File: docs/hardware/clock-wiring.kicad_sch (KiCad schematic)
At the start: 6 parts, among them U1 ESP32 USB-C, U2 5 V logic buffer*, U3 MAX7219 / INPUT, U4 AHT20 + BMP280, U5 NS4168 amplifier

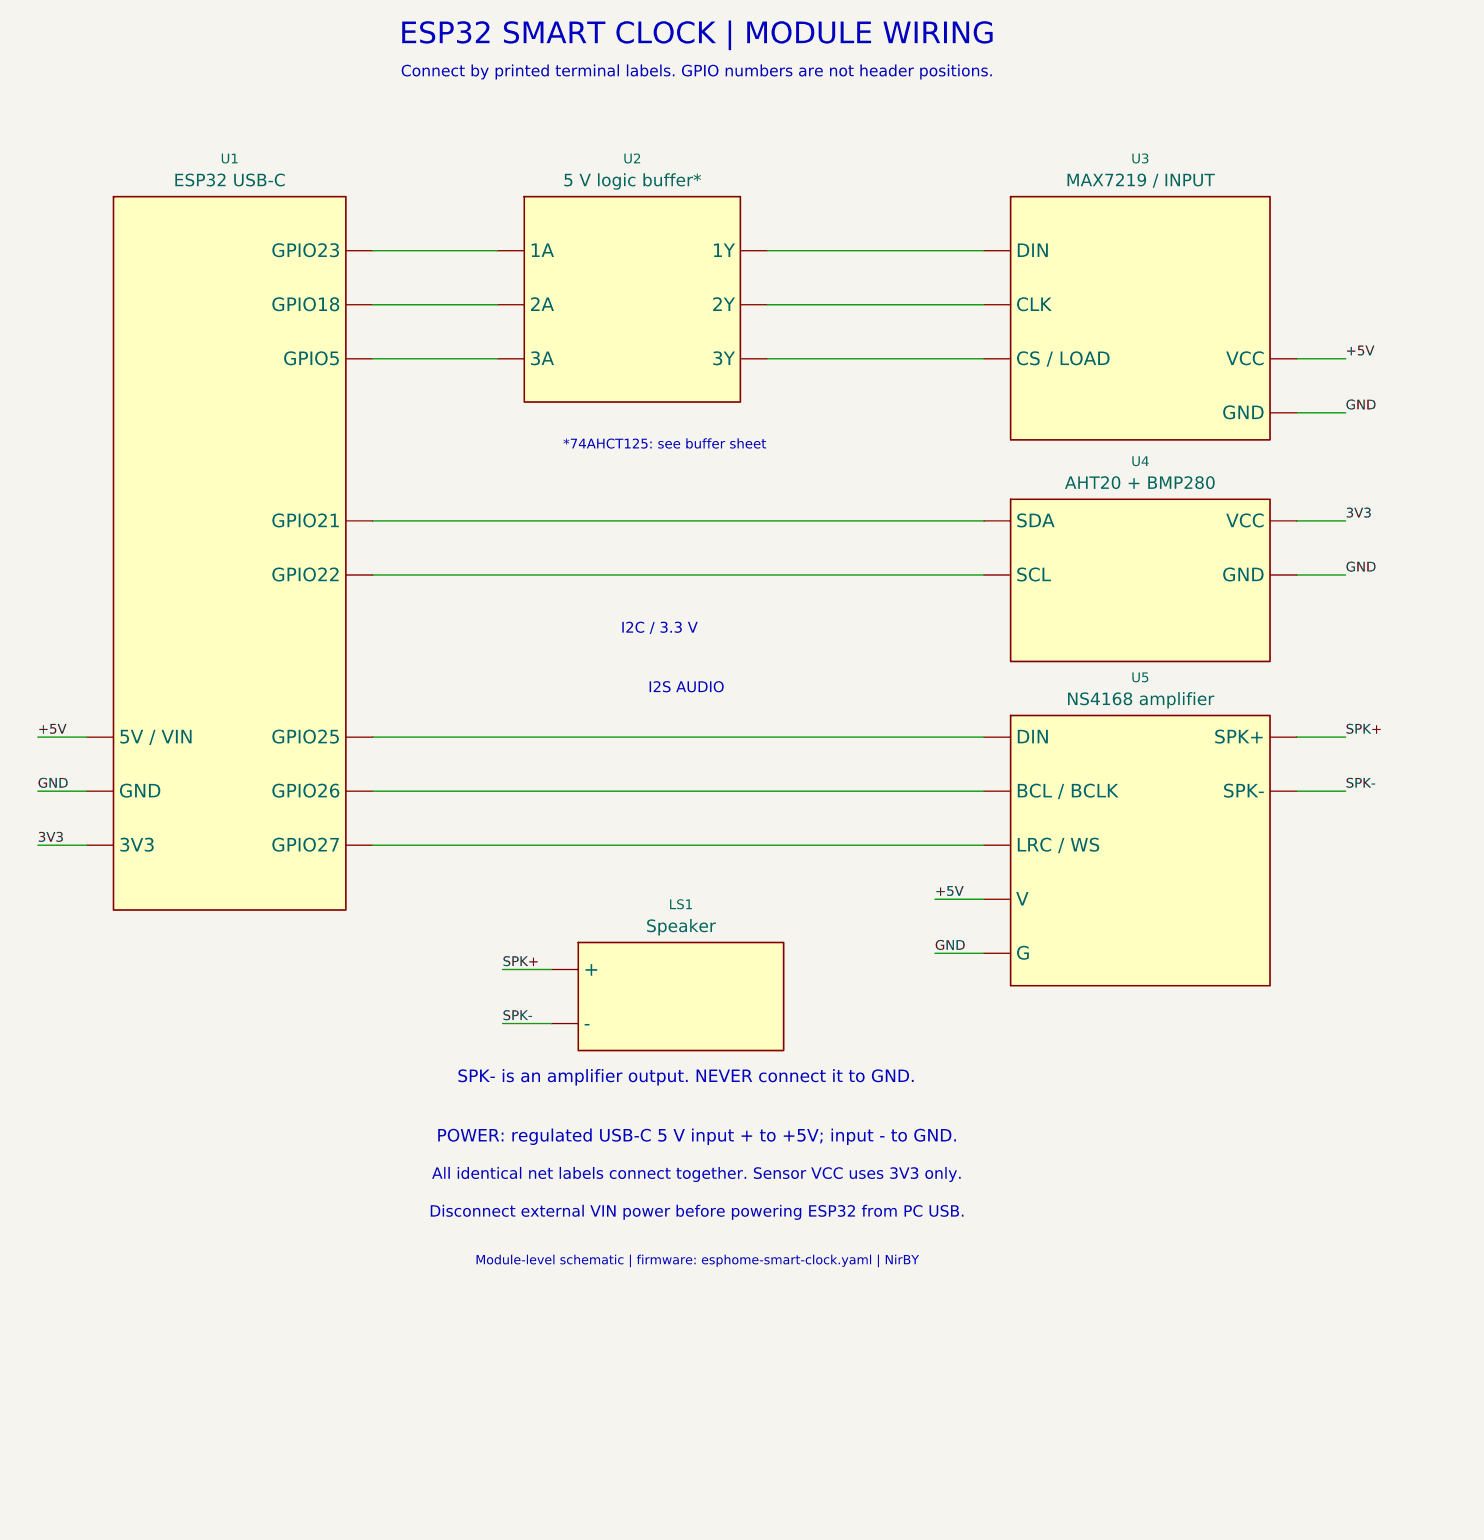
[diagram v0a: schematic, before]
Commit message: Show both USB-C connectors explicitly in wiring diagram
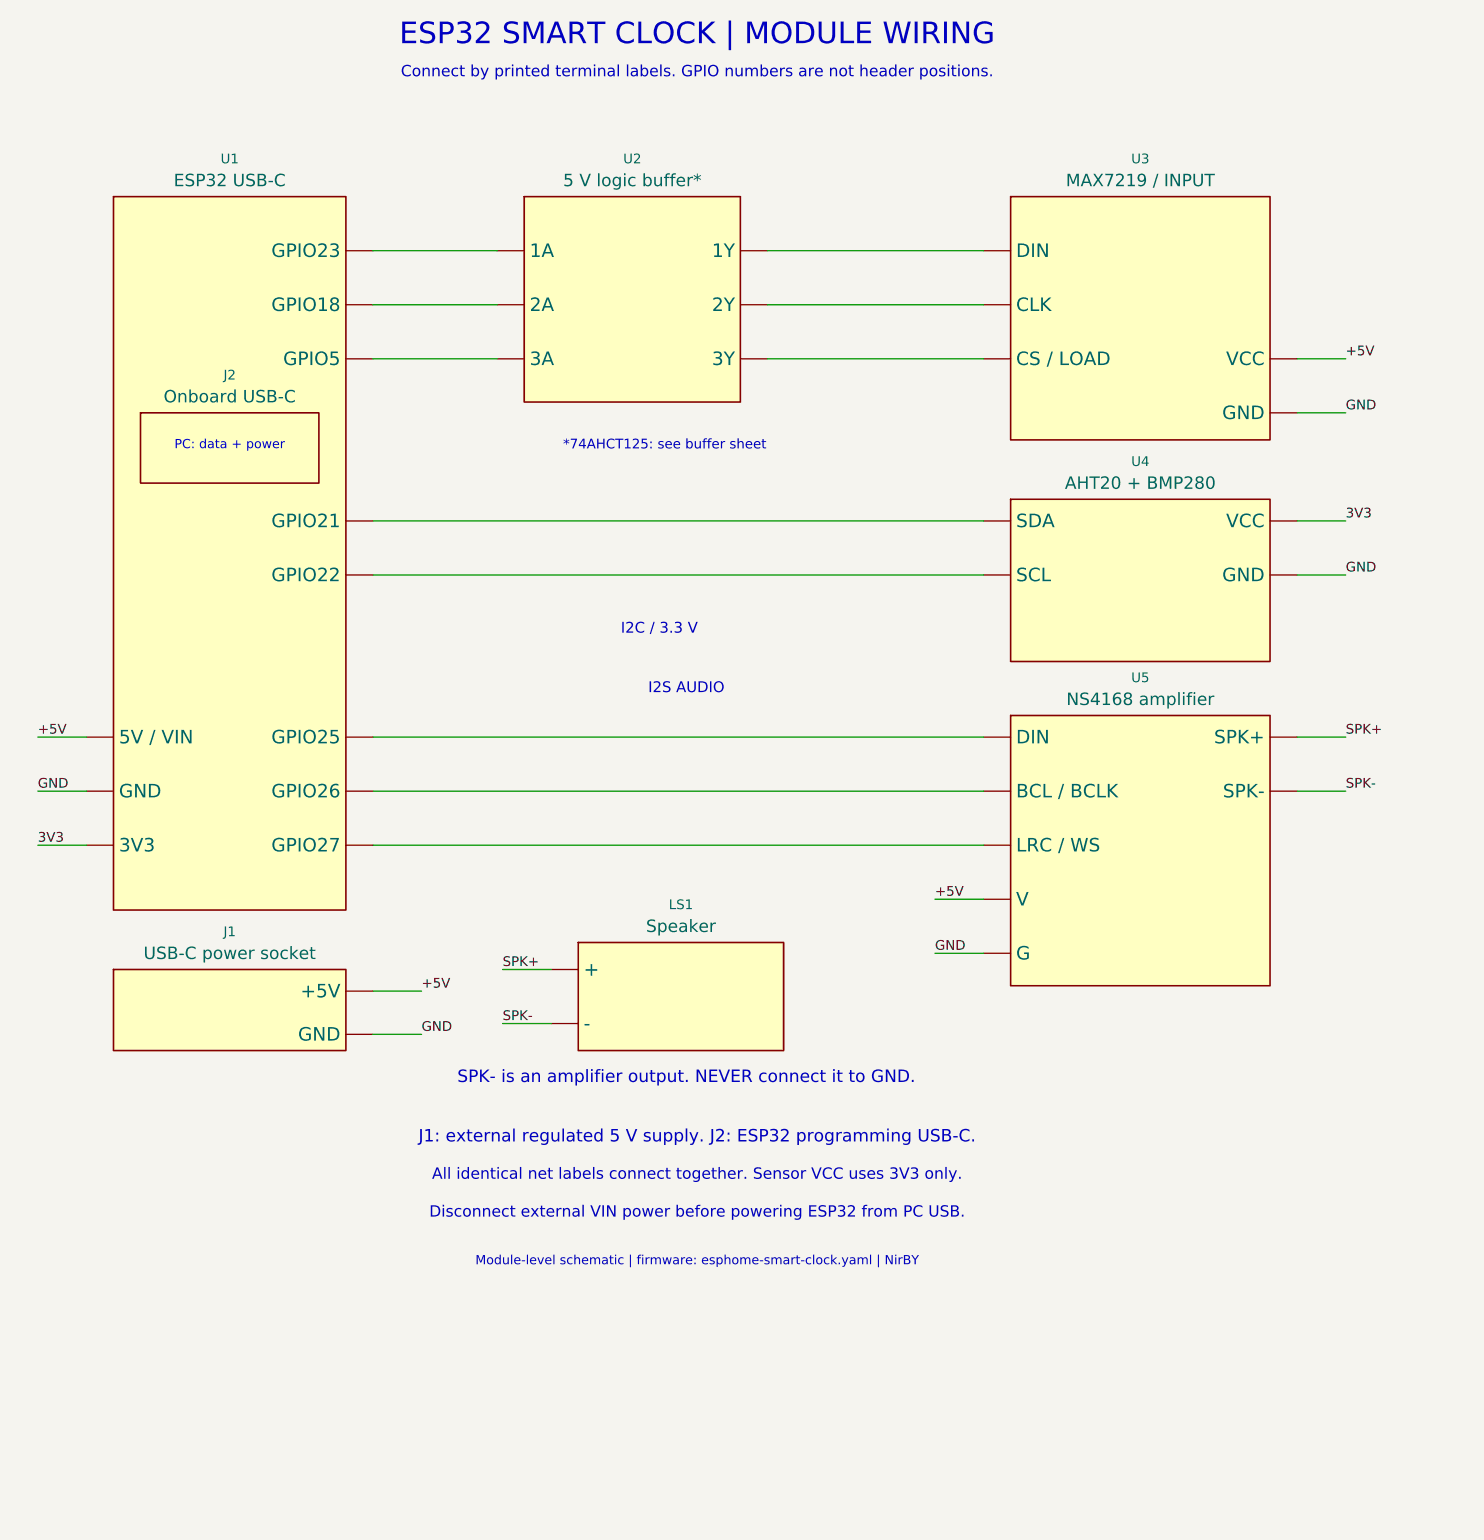
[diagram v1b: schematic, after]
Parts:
- added J1: USB-C power socket, symbol Clock:J1_module
- added J2: Onboard USB-C, symbol Clock:J2_module
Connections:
- net +5V: now also J1.1 (+5V)
- net GND: now also J1.2 (GND)
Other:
- note added: "J1: external regulated 5 V supply. J2: ESP32 programming USB-C."
- note added: "PC: data + power"
- note removed: "POWER: regulated USB-C 5 V input + to +5V; input - to GND."

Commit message: Remove nonexistent U2 and document direct MAX7219 wiring
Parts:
- removed U2: 5 V logic buffer*, symbol Clock:U2_module
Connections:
- net at U1.1 (GPIO23): now also U3.1 (DIN)
- net at U1.2 (GPIO18): now also U3.2 (CLK)
- net at U1.3 (GPIO5): now also U3.3 (CS / LOAD)
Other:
- note added: "DIRECT DISPLAY SIGNALS"
- note removed: "*74AHCT125: see buffer sheet"

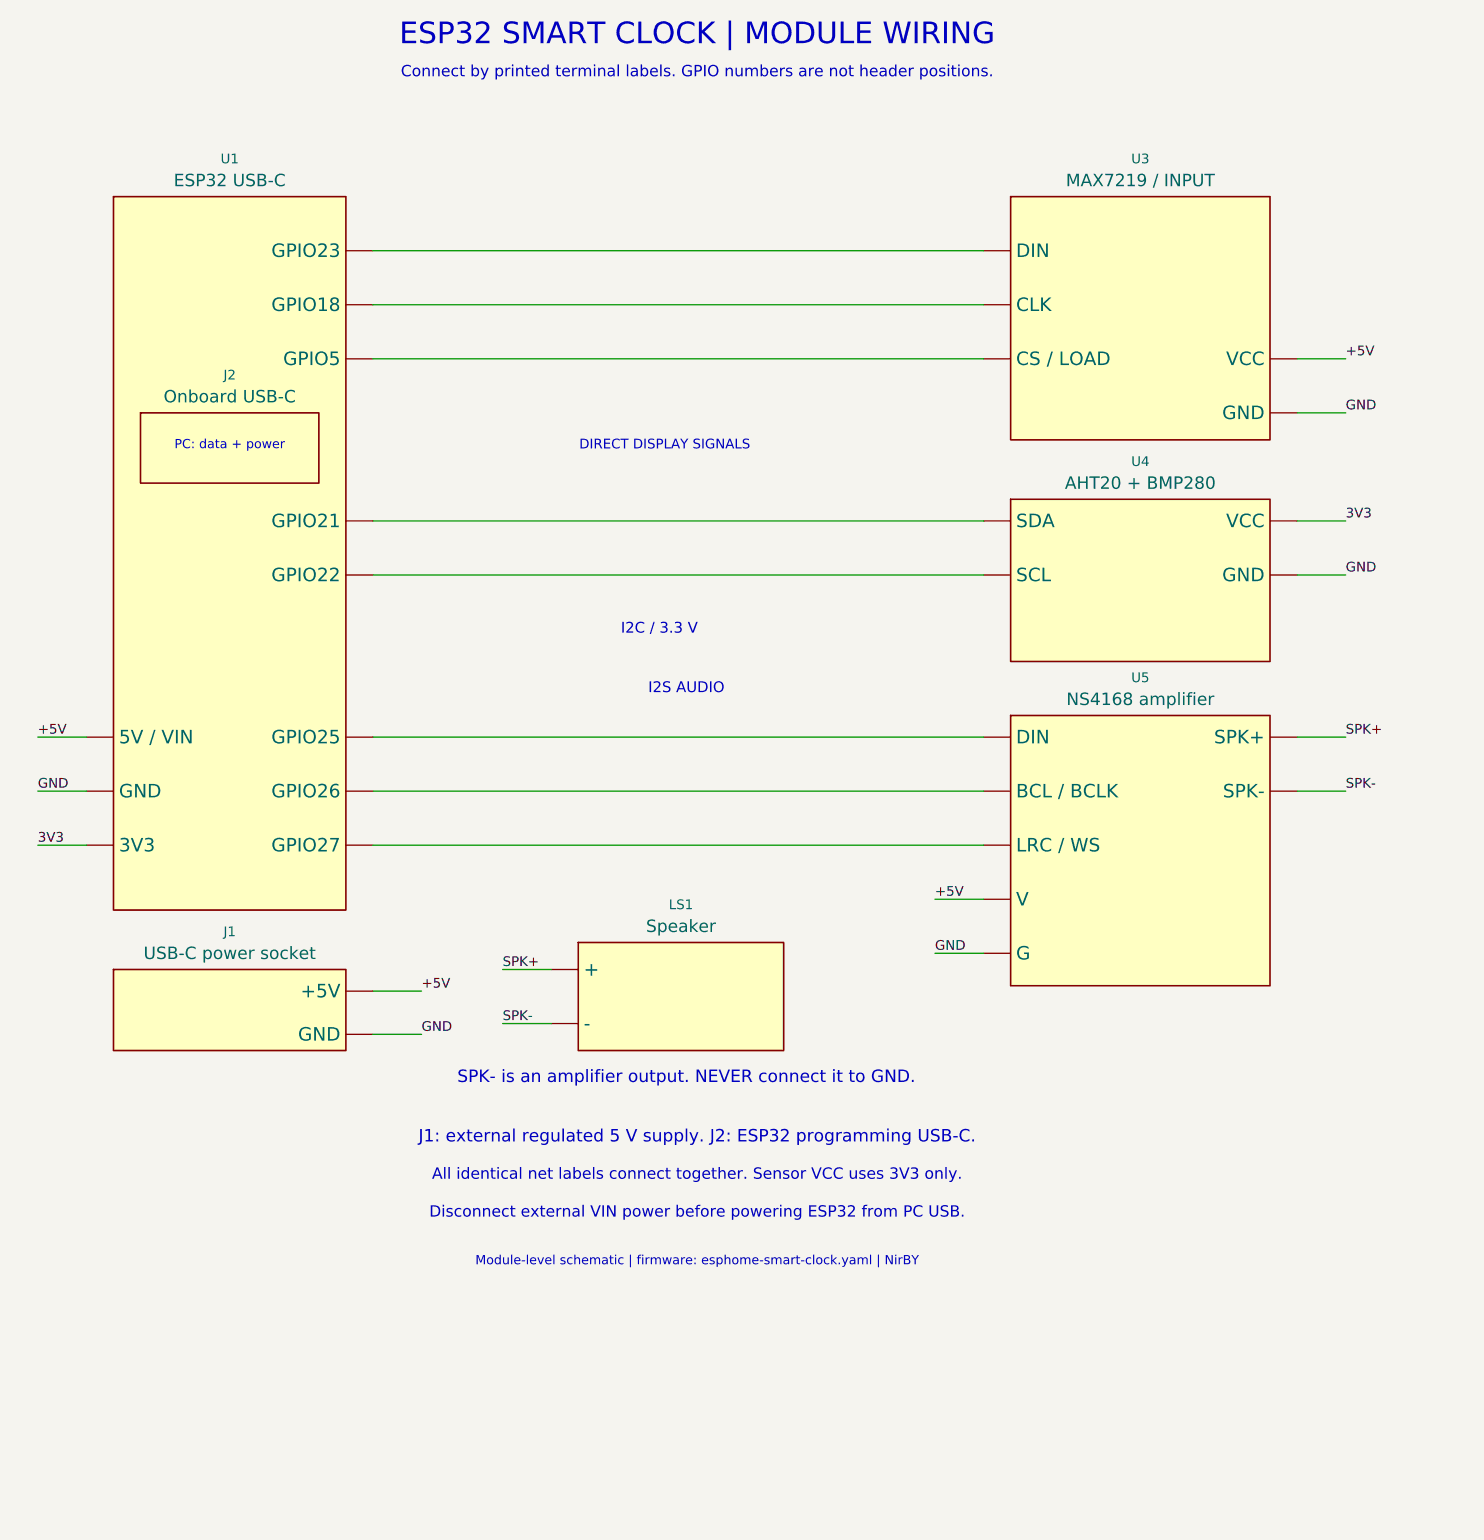
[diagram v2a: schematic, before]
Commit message: Connect USB-C power visibly to all loads in main wiring diagram
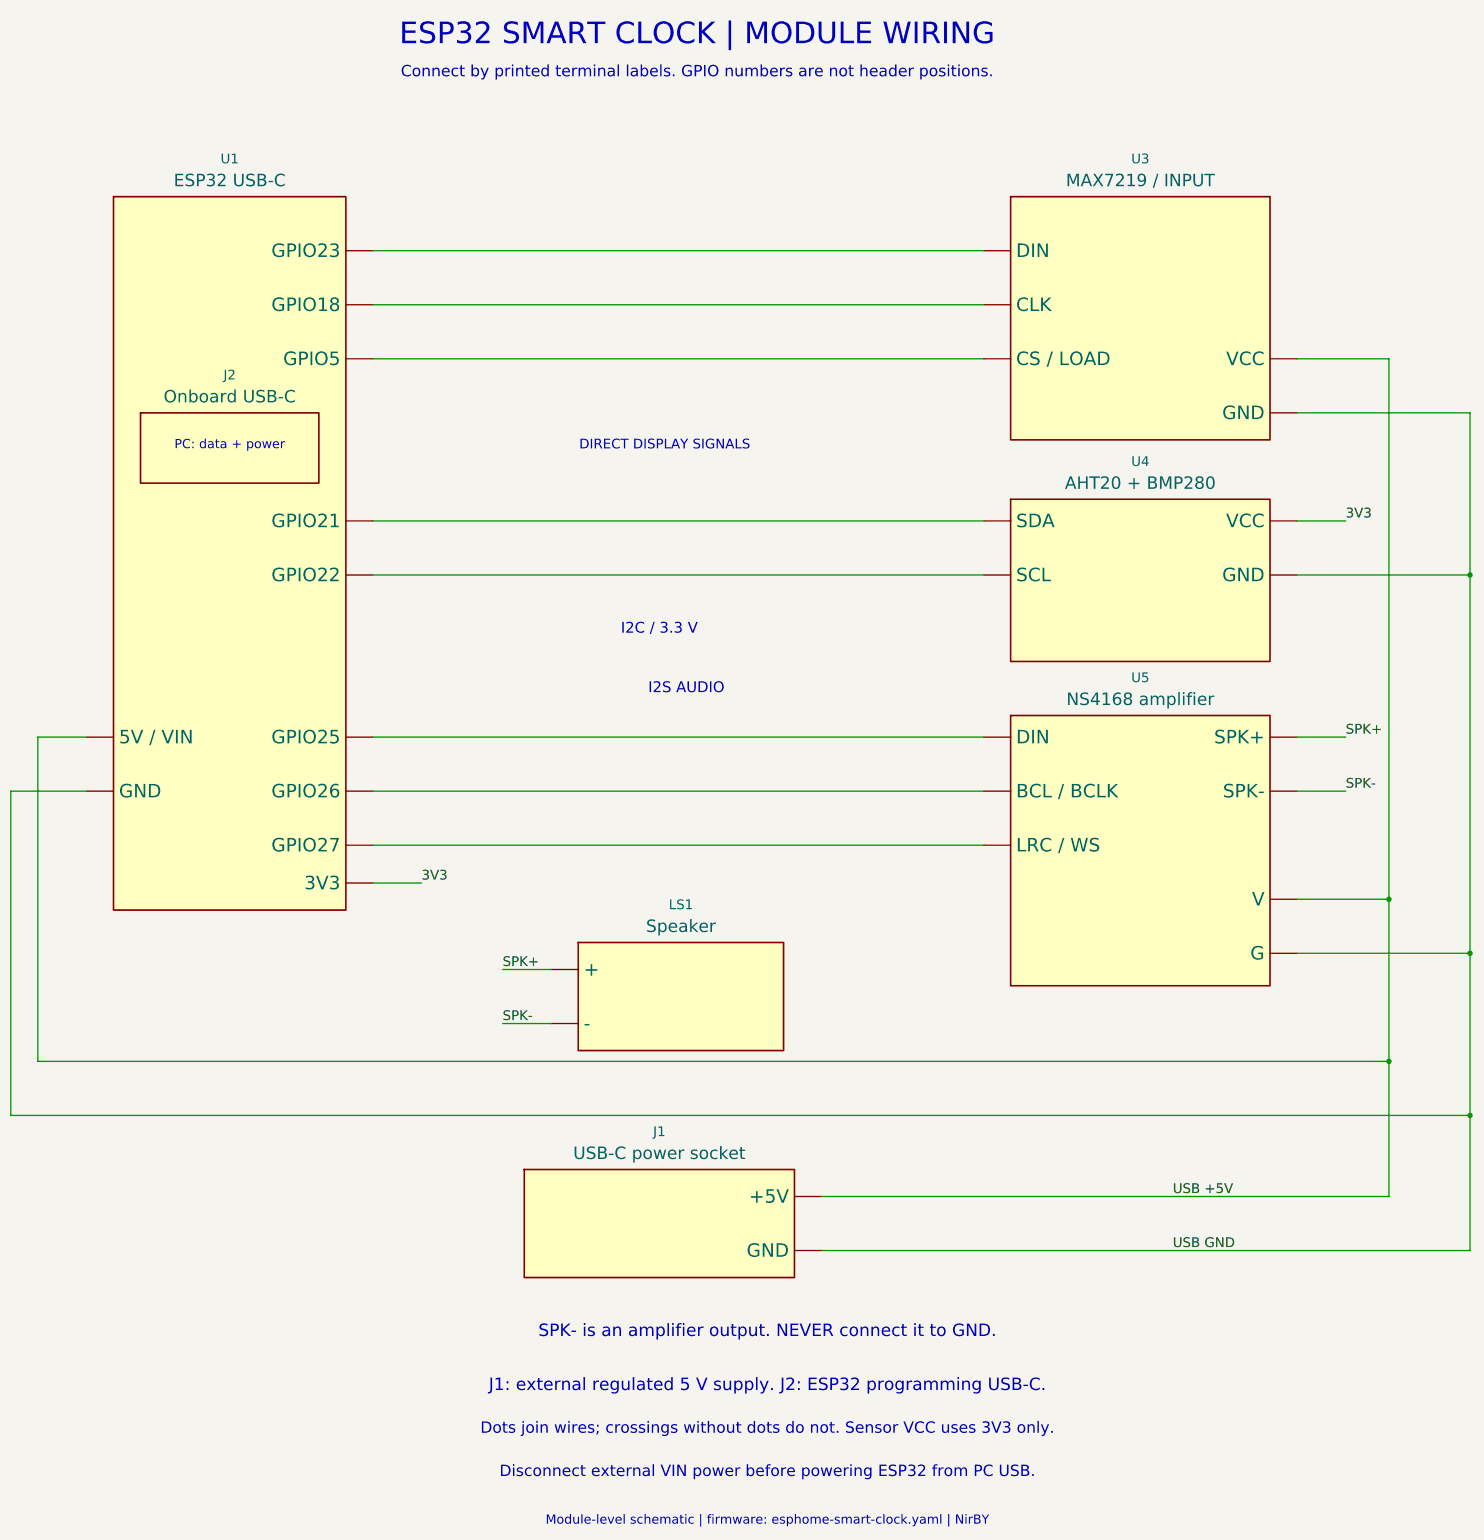
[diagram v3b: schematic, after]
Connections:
- net +5V renamed USB +5V
- net GND renamed USB GND
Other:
- note added: "Dots join wires; crossings without dots do not. Sensor VCC uses 3V3 only."
- note removed: "All identical net labels connect together. Sensor VCC uses 3V3 only."
- moved on the sheet: J1
